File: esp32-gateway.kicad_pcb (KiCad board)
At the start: 2 copper layers, 55 x 95 mm, 36 parts, among them J1 USB_B_Micro, J2 Conn_Coaxial, J3 Ext LED header, J4 Header Left, J5 Header Right, Q1 Q_NPN_BEC, Q2 Q_NPN_BEC, SW1 SW_RESET, SW2 SW_BOOT, SW3 SW_INCLUSION, SW4 SW_GEN1, U1 ESP-WROOM-32, U2 AMS1117-3.3, U3 CH340G, U4 RFM69HCW, U5 RFM69CW, U6 RFM69(H)W, U7 NRF24L01_Breakout, Y1 Crystal 12Mhz

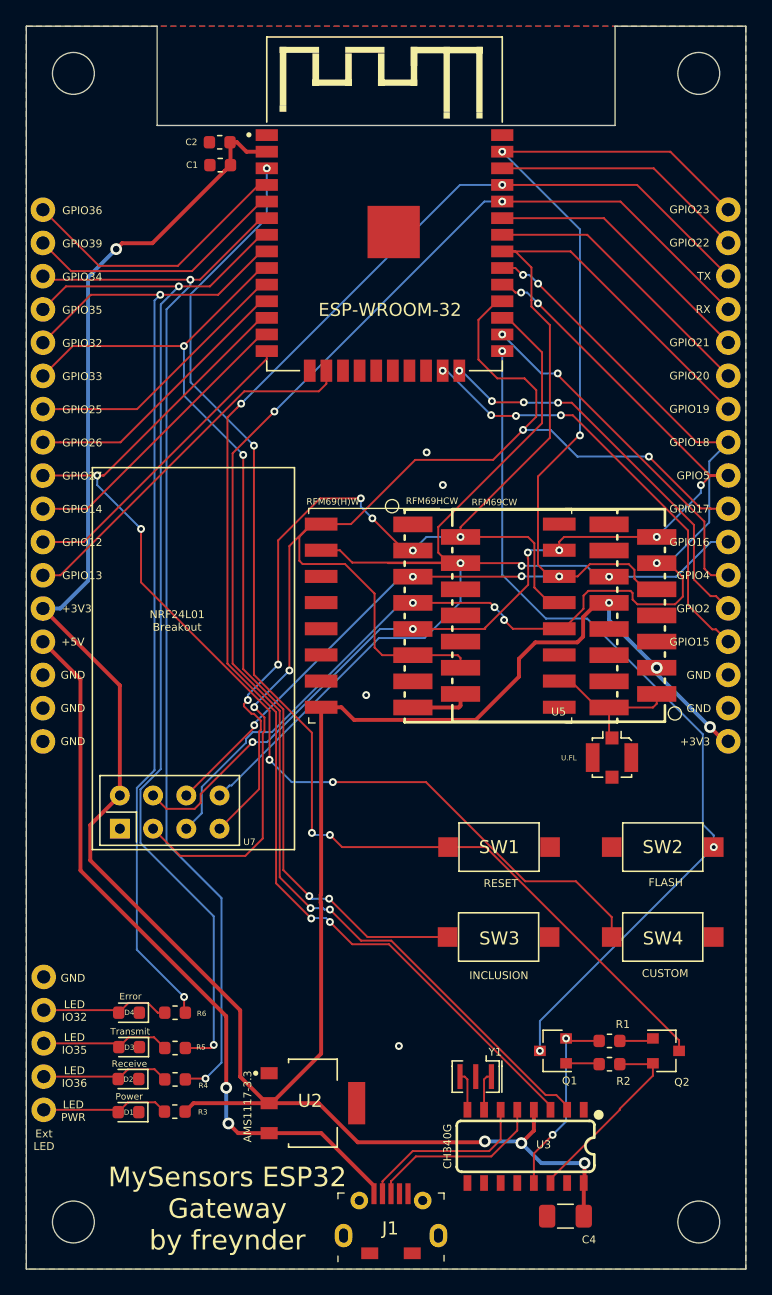
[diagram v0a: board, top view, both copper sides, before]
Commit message: Added readme, optimized traces, added decoupling capacitors
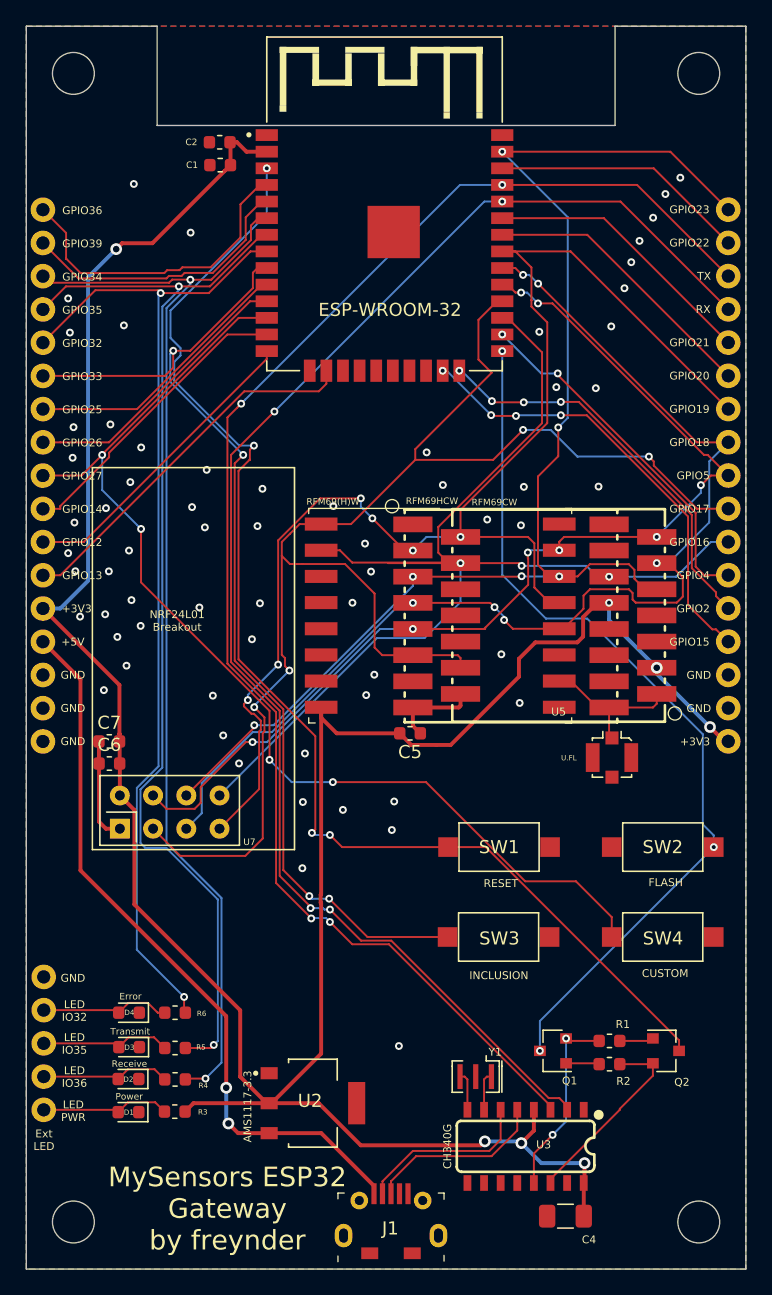
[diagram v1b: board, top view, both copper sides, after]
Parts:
- added C5: 0.1uF, Capacitor_SMD:C_0603_1608Metric, F.Cu at (144.3, 119.0)
- added C6: 10nF, Capacitor_SMD:C_0603_1608Metric, F.Cu at (121.3, 121.4)
- added C7: 1nF, Capacitor_SMD:C_0603_1608Metric, F.Cu at (121.3, 119.7)
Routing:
- net GND: track 4.60 -> 14.8 mm, vias 4 -> 65
- net EN: track 92.5 -> 96.0 mm
- net SENSOR_VP: track 21.4 -> 24.5 mm
- net IO33: track 78.4 -> 80.6 mm
- net SENSOR_VN: track 20.2 -> 21.7 mm
- net IO27: track 81.9 -> 83.4 mm
- net IO35: track 83.3 -> 84.5 mm
- net +3V3: track 208.0 -> 209.1 mm
- net IO34: track 85.2 -> 86.0 mm
- net IO15: track 33.8 -> 34.4 mm

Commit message: Some small trace optimizations
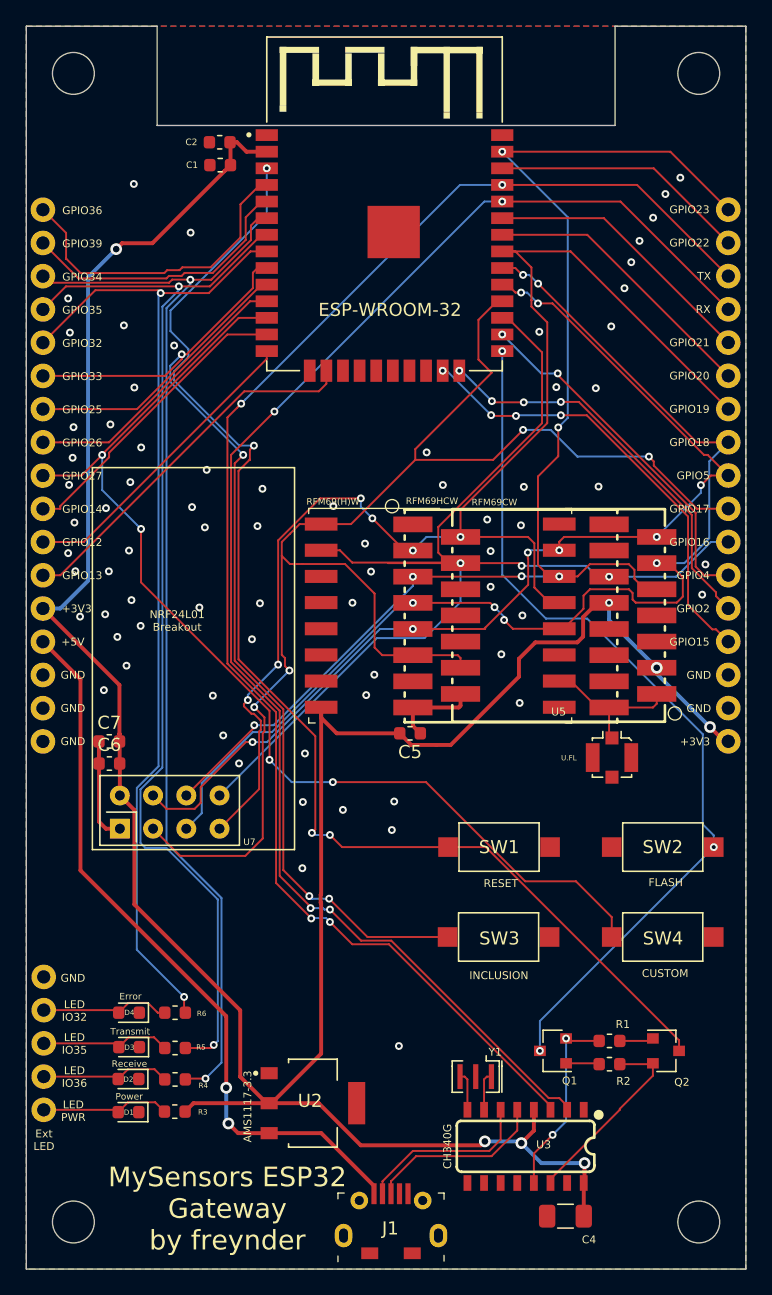
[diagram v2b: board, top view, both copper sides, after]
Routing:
- net IO18: track 88.9 -> 89.6 mm
- net IO33: track 80.6 -> 80.0 mm
- net EN: track 96.0 -> 96.5 mm
- net GND: vias 65 -> 73
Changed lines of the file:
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@@
     (thickness 1.6)
     (drawings 101)
-    (tracks 753)
+    (tracks 761)
     (zones 0)
     (modules 39)
@@
       (drillshape 0)
       (scaleselection 1)
-      (outputdirectory "./gerber_protel"))
+      (outputdirectory "gerber_protel/"))
   )
   (net 0 "")
@@
   (via (at 131.26 121.35) (size 0.6) (drill 0.3) (layers F.Cu B.Cu) (net 1))
   (via (at 155.51 92.59) (size 0.6) (drill 0.3) (layers F.Cu B.Cu) (net 1))
+  (via (at 126.3 89.41) (size 0.6) (drill 0.3) (layers F.Cu B.Cu) (net 1))
+  (via (at 123.26 92.62) (size 0.6) (drill 0.3) (layers F.Cu B.Cu) (net 1))
+  (via (at 118.27 100.06) (size 0.6) (drill 0.3) (layers F.Cu B.Cu) (net 1))
+  (via (at 166.66 108.45) (size 0.6) (drill 0.3) (layers F.Cu B.Cu) (net 1))
+  (via (at 150.49 107.85) (size 0.6) (drill 0.3) (layers F.Cu B.Cu) (net 1))
+  (via (at 150.49 105.12) (size 0.6) (drill 0.3) (layers F.Cu B.Cu) (net 1))
+  (via (at 152.92 110.04) (size 0.6) (drill 0.3) (layers F.Cu B.Cu) (net 1))
+  (via (at 166.91 106.14) (size 0.6) (drill 0.3) (layers F.Cu B.Cu) (net 1))
   (via (at 159.54 109.07) (size 0.6) (drill 0.3) (layers F.Cu B.Cu) (net 2) (status 30))
   (via (at 163.186 114.038) (size 0.9) (drill 0.5) (layers F.Cu B.Cu) (net 2) (status 30))
@@
   (segment (start 131.22 98.99) (end 131.22 113.392992) (width 0.15) (layer F.Cu) (net 10))
   (segment (start 131.22 113.392992) (end 137.09 119.262992) (width 0.15) (layer F.Cu) (net 10))
-  (segment (start 126.02 86.74) (end 133.38 79.38) (width 0.15) (layer B.Cu) (net 10))
-  (segment (start 131.28 97.06) (end 126.31 92.09) (width 0.15) (layer B.Cu) (net 10))
-  (segment (start 132.4 97.06) (end 131.28 97.06) (width 0.15) (layer B.Cu) (net 10))
-  (segment (start 126.79 90.17) (end 126.79 89.6) (width 0.15) (layer B.Cu) (net 10))
-  (segment (start 133.38 79.38) (end 133.38 75.865) (width 0.15) (layer B.Cu) (net 10))
-  (segment (start 126.31 92.09) (end 126.31 90.65) (width 0.15) (layer B.Cu) (net 10))
-  (segment (start 126.79 89.6) (end 126.02 88.83) (width 0.15) (layer B.Cu) (net 10))
-  (segment (start 126.02 88.83) (end 126.02 86.74) (width 0.15) (layer B.Cu) (net 10))
-  (segment (start 126.31 90.65) (end 126.79 90.17) (width 0.15) (layer B.Cu) (net 10))
+  (segment (start 126.28 92.06) (end 131.28 97.06) (width 0.15) (layer B.Cu) (net 10))
+  (segment (start 133.38 79.38) (end 126.02 86.74) (width 0.15) (layer B.Cu) (net 10))
+  (segment (start 126.28 91.4) (end 126.28 92.06) (width 0.15) (layer B.Cu) (net 10))
+  (segment (start 133.38 75.865) (end 133.38 79.38) (width 0.15) (layer B.Cu) (net 10))
+  (segment (start 126.02 86.74) (end 126.02 88.31) (width 0.15) (layer B.Cu) (net 10))
+  (segment (start 126.02 88.31) (end 127.39 89.68) (width 0.15) (layer B.Cu) (net 10))
+  (segment (start 131.28 97.06) (end 132.4 97.06) (width 0.15) (layer B.Cu) (net 10))
+  (segment (start 127.39 89.68) (end 127.39 90.29) (width 0.15) (layer B.Cu) (net 10))
+  (segment (start 127.39 90.29) (end 126.28 91.4) (width 0.15) (layer B.Cu) (net 10))
   (segment (start 155.067 153.12136) (end 160.36286 147.8255) (width 0.15) (layer F.Cu) (net 11) (status 10))
   (segment (start 155.067 153.42108) (end 155.067 153.12136) (width 0.15) (layer F.Cu) (net 11) (status 30))
@@
   (segment (start 136.63 131.49) (end 134.646021 129.506021) (width 0.15) (layer F.Cu) (net 17))
   (segment (start 134.646021 129.506021) (end 134.646021 117.210765) (width 0.15) (layer F.Cu) (net 17))
+  (segment (start 126 92.19) (end 131.58 97.77) (width 0.15) (layer B.Cu) (net 17))
+  (segment (start 126.88 90.08) (end 126 90.96) (width 0.15) (layer B.Cu) (net 17))
+  (segment (start 126.88 90.45) (end 125.6 91.73) (width 0.15) (layer F.Cu) (net 17))
+  (segment (start 126.88 90.08) (end 126.88 90.45) (width 0.15) (layer F.Cu) (net 17))
+  (segment (start 126 90.96) (end 126 92.19) (width 0.15) (layer B.Cu) (net 17))
+  (segment (start 126.88 90.08) (end 127.26 90.08) (width 0.15) (layer F.Cu) (net 17))
+  (segment (start 125.6 91.73) (end 116.27 91.73) (width 0.15) (layer F.Cu) (net 17))
+  (segment (start 132.32 85.02) (end 132.32 83.84) (width 0.15) (layer F.Cu) (net 17))
+  (segment (start 127.26 90.08) (end 132.32 85.02) (width 0.15) (layer F.Cu) (net 17))
+  (via (at 126.88 90.08) (size 0.6) (drill 0.3) (layers F.Cu B.Cu) (net 17))
+  (segment (start 132.675 83.485) (end 133.38 83.485) (width 0.15) (layer F.Cu) (net 17))
   (segment (start 132.32 83.84) (end 132.675 83.485) (width 0.15) (layer F.Cu) (net 17))
-  (segment (start 126.23 89.81) (end 127.53 89.81) (width 0.15) (layer F.Cu) (net 17))
-  (segment (start 125.6 91.73) (end 116.27 91.73) (width 0.15) (layer F.Cu) (net 17))
-  (segment (start 127.53 89.81) (end 132.32 85.02) (width 0.15) (layer F.Cu) (net 17))
-  (segment (start 132.675 83.485) (end 133.38 83.485) (width 0.15) (layer F.Cu) (net 17))
-  (segment (start 132.32 85.02) (end 132.32 83.84) (width 0.15) (layer F.Cu) (net 17))
-  (segment (start 126.23 89.81) (end 126.23 91.1) (width 0.15) (layer F.Cu) (net 17))
-  (via (at 126.23 89.81) (size 0.6) (drill 0.3) (layers F.Cu B.Cu) (net 17))
-  (segment (start 126.23 91.1) (end 125.6 91.73) (width 0.15) (layer F.Cu) (net 17))
-  (segment (start 126 92.19) (end 131.58 97.77) (width 0.15) (layer B.Cu) (net 17))
-  (segment (start 126.23 89.81) (end 126 90.04) (width 0.15) (layer B.Cu) (net 17))
-  (segment (start 126 90.04) (end 126 92.19) (width 0.15) (layer B.Cu) (net 17))
   (segment (start 117.599077 94.27) (end 116.27 94.27) (width 0.15) (layer F.Cu) (net 18))
   (segment (start 123.465 94.27) (end 117.599077 94.27) (width 0.15) (layer F.Cu) (net 18))
@@
   (segment (start 153.45 84.01) (end 154.12 84.68) (width 0.15) (layer B.Cu) (net 36))
   (via (at 163.186 106.04208) (size 0.6) (drill 0.3) (layers F.Cu B.Cu) (net 36) (status 30))
-  (segment (start 167.2 98.26) (end 168.656 96.804) (width 0.15) (layer B.Cu) (net 36) (status 20))
-  (segment (start 167.2 102.92851) (end 167.2 98.26) (width 0.15) (layer B.Cu) (net 36))
-  (segment (start 164.08643 106.04208) (end 167.2 102.92851) (width 0.15) (layer B.Cu) (net 36))
-  (segment (start 163.186 106.04208) (end 164.08643 106.04208) (width 0.15) (layer B.Cu) (net 36))
   (segment (start 133.769272 118.957998) (end 143.64749 109.07978) (width 0.15) (layer B.Cu) (net 36))
   (segment (start 132.312861 118.957998) (end 133.769272 118.957998) (width 0.15) (layer B.Cu) (net 36))
@@
   (segment (start 161.58 109.06) (end 161.34 108.82) (width 0.15) (layer F.Cu) (net 36))
   (segment (start 164.72 109.06) (end 161.58 109.06) (width 0.15) (layer F.Cu) (net 36))
+  (segment (start 167.2 98.26) (end 168.656 96.804) (width 0.15) (layer B.Cu) (net 36))
+  (segment (start 167.2 104.14) (end 167.2 98.26) (width 0.15) (layer B.Cu) (net 36))
+  (segment (start 163.186 106.04208) (end 165.29792 106.04208) (width 0.15) (layer B.Cu) (net 36))
+  (segment (start 165.29792 106.04208) (end 167.2 104.14) (width 0.15) (layer B.Cu) (net 36))
   (via (at 148.18984 104.04056) (size 0.6) (drill 0.3) (layers F.Cu B.Cu) (net 37) (status 30))
   (via (at 144.54792 105.07928) (size 0.6) (drill 0.3) (layers F.Cu B.Cu) (net 37) (status 30))

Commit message: Fixed initial issues and made font larger.
Issues fixed are:
- TX and RX LEDs connected to IO34 and IO35 do not work as ESP32 does not support pull-up on those pins.
- Wrong labeling of RX led (mentioned 36 but should be 34)
- C4 capacitor was located near the CH340G chip but should have been near AMS1117
- Missing pull-up on EN pin.
- Missing capacitor to ground on EN pin.
- auto flash does not work due to missing pull-up on EN pin.
- corners need slight filing to fit in enclosure
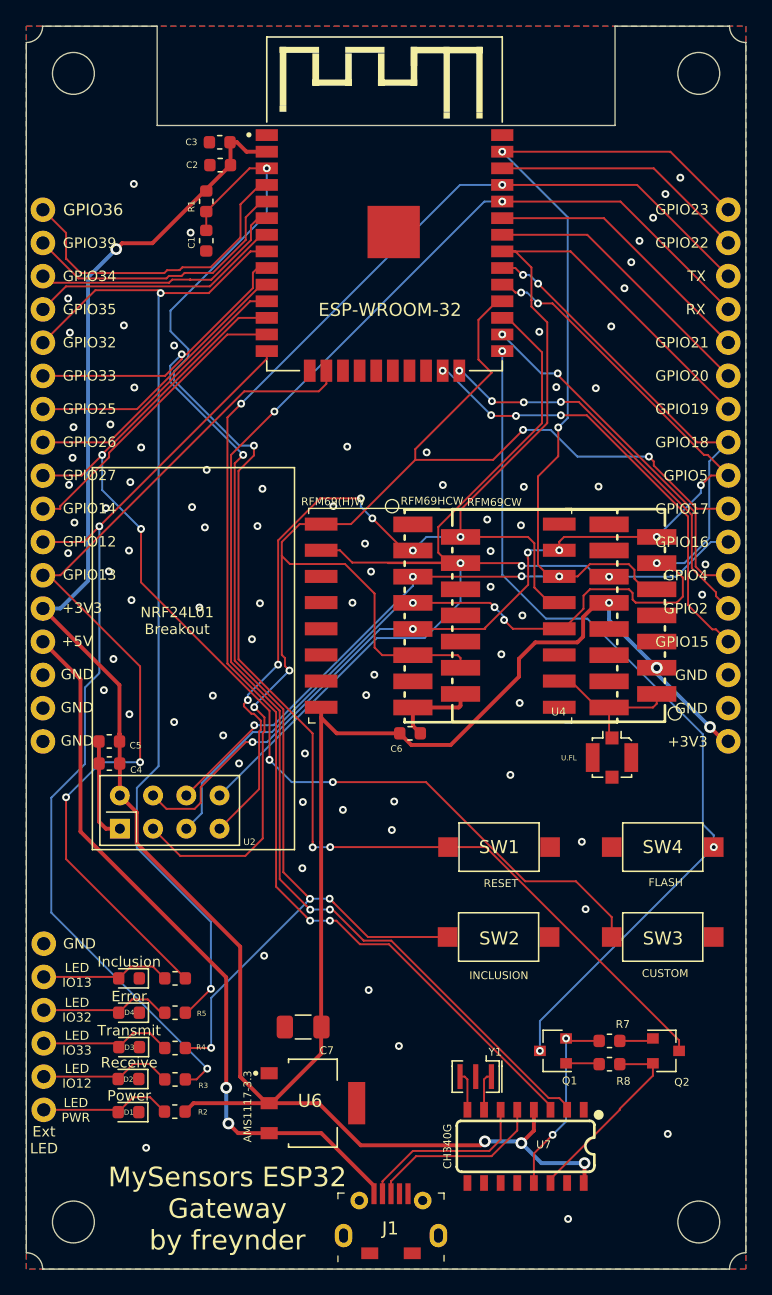
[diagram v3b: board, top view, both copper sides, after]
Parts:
- removed the U7 at (122.2, 126.3)
- added C1: 0.1uF, Capacitor_SMD:C_0603_1608Metric, F.Cu at (128.8, 81.4)
- added D5: LED WHITE, LED_SMD:LED_0603_1608Metric, F.Cu at (122.8, 137.8)
- added R1: 10K, Resistor_SMD:R_0603_1608Metric, F.Cu at (128.8, 78.4)
- added R6: 22, Resistor_SMD:R_0603_1608Metric, F.Cu at (126.4, 137.8)
- added U2: NRF24L01_Breakout, RF_Module:nRF24L01_Breakout, F.Cu at (122.2, 126.3)
- J3: footprint Sparkfun Connectors:1X05_NO_SILK -> Sparkfun Connectors:1X06_NO_SILK
- moved C7 24.7 mm to (136.2, 141.5)
- renumbered C1 to C2, C2 to C3, C6 to C4, C7 to C5, C5 to C6, C4 to C7, R3 to R2, R4 to R3, R5 to R4, R6 to R5, R1 to R7, R2 to R8, SW3 to SW2, SW4 to SW3, SW2 to SW4, U4 to U1, U1 to U3, U5 to U4, U6 to U5, U2 to U6, U3 to U7
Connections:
- J3 pad 5: GND -> Net-(D5-Pad2)
- R3 pad 2: IO34 -> IO12
- R4 pad 2: IO35 -> IO33
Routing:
- net IO34: track 86.0 -> 20.4 mm, vias 2 -> 0
- net IO35: track 84.5 -> 19.5 mm, vias 2 -> 0
- net IO12: track 23.5 -> 73.4 mm, vias 0 -> 2
- net IO13: track 28.7 -> 70.8 mm, vias 0 -> 2
- net IO33: track 80.0 -> 96.6 mm, vias 4 -> 5
- net Net-(D5-Pad2): track 0.00 -> 10.0 mm
- net EN: track 96.5 -> 104.4 mm
- net +3V3: track 209.1 -> 205.7 mm
- net IO32: track 77.5 -> 79.2 mm
- net GND: vias 73 -> 79
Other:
- outline, holes or cut-outs redrawn
- board text added: "Inclusion"
- board text added: "LED IO12"
- board text added: "LED IO13"
- board text added: "LED IO33"
- board text removed: "LED IO35"
- board text removed: "LED IO36"
